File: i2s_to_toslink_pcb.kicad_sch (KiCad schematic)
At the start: 0 parts

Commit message: printed pdf from schematics
Signed-off-by: Mika Laitio <lamikr@gmail.com>
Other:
- company: (none) -> Mika Laitio
- title: (none) -> I2S Audio to AES/EBU Optical Toslink
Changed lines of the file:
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@@
   (paper "A4")
   (title_block
+    (title "I2S Audio to AES/EBU Optical Toslink")
     (date "2023-12-26")
     (rev "v0.1")
+    (company "Mika Laitio")
   )
   (sheet (at 26.67 22.86) (size 41.91 29.21) (fields_autoplaced)

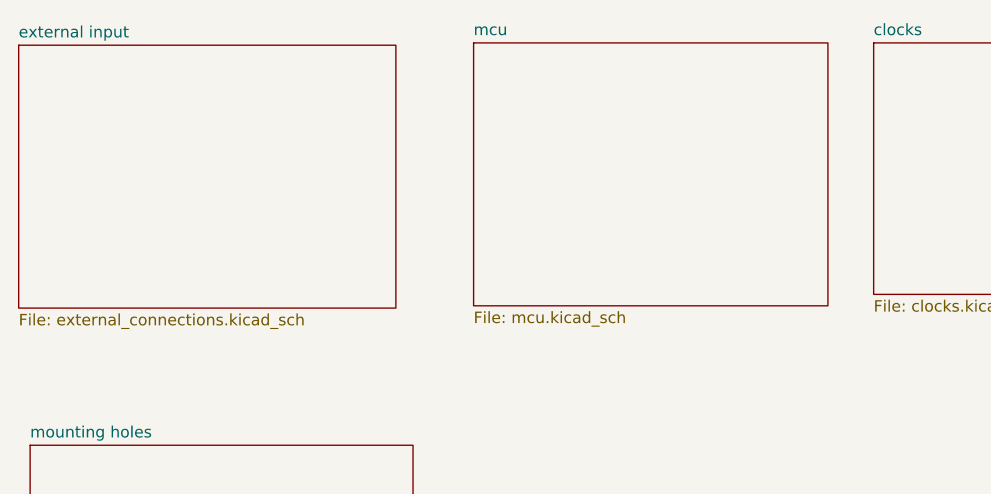
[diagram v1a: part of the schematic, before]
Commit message: various updates
- removed duplicates 5V power connectors
- now the whole pcb is always powered via 6 pin
  atmega avr isp connector
- added connector for wm8805 rx0 and rx1
- added labels for jumpers/connectors
- moved the orientation of existing connecors
- moved the location of ldo close to
  6 pin avr isp connector

Signed-off-by: Mika Laitio <lamikr@gmail.com>
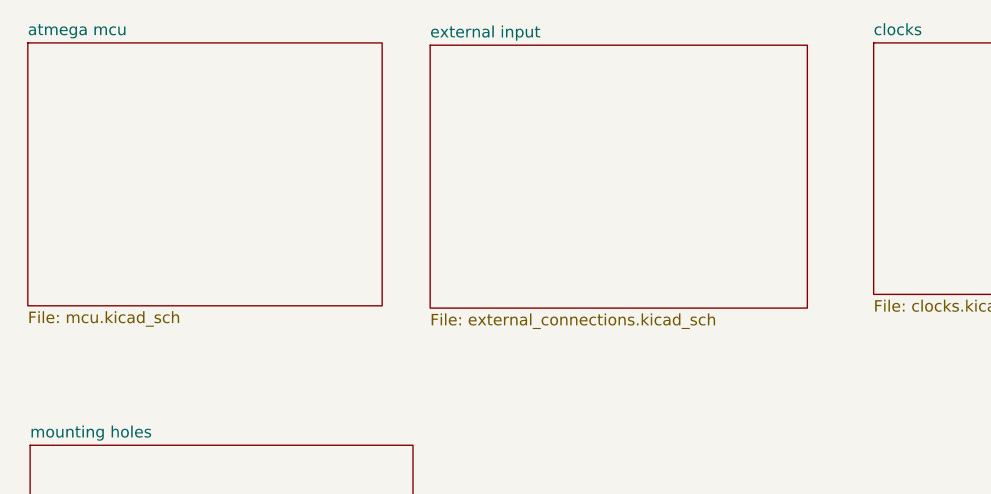
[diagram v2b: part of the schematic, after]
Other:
- sheet mcu renamed atmega mcu
